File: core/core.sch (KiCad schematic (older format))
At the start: 52 parts, among them J1 Micro_SD_Card, J2 UART_DEBUG, J3 Conn_ARM_JTAG_SWD_10, J4 Conn_01x02, J5 USB_OTG, SW1 SW_Push, SW2 SW_Push, U1 SC18IS600, U2 AP1509-50, U3 AP1509-33

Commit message: update layout
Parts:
- removed TP1, TP10, TP11, TP5, TP7: TestPoint, TestPoint:TestPoint_Keystone_5010-5014_Multipurpose, symbol Connector:TestPoint
- J2: footprint star-common-lib:TSM-103-01-L-SV -> Connector_PinHeader_2.54mm:PinHeader_1x03_P2.54mm_Vertical; DIGIKEY SAM8981-ND -> 609-3470-ND; MANF TSM-103-01-L-SV -> 68001-203HLF
- SW1, SW2: footprint Button_Switch_SMD:SW_SPST_CK_RS282G05A3 -> Button_Switch_SMD:SW_SPST_PTS810; DIGIKEY CKN10384CT-ND -> CKN10502CT-ND; MANF RS-282G05A3-SM RT -> PTS810 SJM 250 SMTR LFS
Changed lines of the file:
@@
 F 0 "SW1" H 5550 2735 50  0000 C CNN
 F 1 "SW_Push" H 5550 2644 50  0000 C CNN
-F 2 "Button_Switch_SMD:SW_SPST_CK_RS282G05A3" H 5550 2650 50  0001 C CNN
+F 2 "Button_Switch_SMD:SW_SPST_PTS810" H 5550 2650 50  0001 C CNN
 F 3 "~" H 5550 2650 50  0001 C CNN
-F 4 "CKN10384CT-ND" H 5550 2450 50  0001 C CNN "DIGIKEY"
-F 5 "RS-282G05A3-SM RT" H 5550 2450 50  0001 C CNN "MANF"
+F 4 "CKN10502CT-ND" H 5550 2450 50  0001 C CNN "DIGIKEY"
+F 5 "PTS810 SJM 250 SMTR LFS" H 5550 2450 50  0001 C CNN "MANF"
 	1    5550 2450
 	1    0    0    -1
@@
 F 0 "J2" H 3758 3181 50  0000 C CNN
 F 1 "UART_DEBUG" H 3758 3090 50  0000 C CNN
-F 2 "star-common-lib:TSM-103-01-L-SV" H 3650 2900 50  0001 C CNN
+F 2 "Connector_PinHeader_2.54mm:PinHeader_1x03_P2.54mm_Vertical" H 3650 2900 50  0001 C CNN
 F 3 "~" H 3650 2900 50  0001 C CNN
 F 4 "" H 3650 2900 50  0001 C CNN "manf#"
-F 5 "TSM-103-01-L-SV" H 3650 2900 50  0001 C CNN "MANF"
-F 6 "SAM8981-ND" H 3650 2900 50  0001 C CNN "DIGIKEY"
+F 5 "68001-203HLF" H 3650 2900 50  0001 C CNN "MANF"
+F 6 "609-3470-ND" H 3650 2900 50  0001 C CNN "DIGIKEY"
 	1    3650 2900
 	1    0    0    -1
@@
 Wire Wire Line
 	4600 1650 4750 1650
-$Comp
-L Connector:TestPoint TP1
-U 1 1 5F25E4E9
-P 10200 3750
-F 0 "TP1" H 10258 3868 50  0000 L CNN
-F 1 "TestPoint" H 10258 3777 50  0000 L CNN
-F 2 "TestPoint:TestPoint_Keystone_5010-5014_Multipurpose" H 10400 3750 50  0001 C CNN
-F 3 "~" H 10400 3750 50  0001 C CNN
-F 4 "36-5014-ND" H 10200 3750 50  0001 C CNN "DIGIKEY"
-F 5 "5014" H 10200 3750 50  0001 C CNN "MANF"
-	1    10200 3750
-	-1   0    0    1
-$EndComp
-$Comp
-L power:+3.3V #PWR040
-U 1 1 5F2D6F88
-P 10200 3750
-F 0 "#PWR040" H 10200 3600 50  0001 C CNN
-F 1 "+3.3V" H 10215 3923 50  0000 C CNN
-F 2 "" H 10200 3750 50  0001 C CNN
-F 3 "" H 10200 3750 50  0001 C CNN
-	1    10200 3750
-	1    0    0    -1
-$EndComp
-$Comp
-L Connector:TestPoint TP7
-U 1 1 5F2D875C
-P 10650 3750
-F 0 "TP7" H 10708 3868 50  0000 L CNN
-F 1 "TestPoint" H 10708 3777 50  0000 L CNN
-F 2 "TestPoint:TestPoint_Keystone_5010-5014_Multipurpose" H 10850 3750 50  0001 C CNN
-F 3 "~" H 10850 3750 50  0001 C CNN
-F 4 "36-5014-ND" H 10650 3750 50  0001 C CNN "DIGIKEY"
-F 5 "5014" H 10650 3750 50  0001 C CNN "MANF"
-	1    10650 3750
-	-1   0    0    1
-$EndComp
-$Comp
-L power:+5V #PWR045
-U 1 1 5F2DA0B7
-P 10650 3750
-F 0 "#PWR045" H 10650 3600 50  0001 C CNN
-F 1 "+5V" H 10665 3923 50  0000 C CNN
-F 2 "" H 10650 3750 50  0001 C CNN
-F 3 "" H 10650 3750 50  0001 C CNN
-	1    10650 3750
-	1    0    0    -1
-$EndComp
 Wire Notes Line
 	6900 2750 6900 3500
@@
 F 0 "SW2" H 6450 1735 50  0000 C CNN
 F 1 "SW_Push" H 6450 1644 50  0000 C CNN
-F 2 "Button_Switch_SMD:SW_SPST_CK_RS282G05A3" H 6450 1650 50  0001 C CNN
+F 2 "Button_Switch_SMD:SW_SPST_PTS810" H 6450 1650 50  0001 C CNN
 F 3 "~" H 6450 1650 50  0001 C CNN
-F 4 "CKN10384CT-ND" H 6450 1450 50  0001 C CNN "DIGIKEY"
-F 5 "RS-282G05A3-SM RT" H 6450 1450 50  0001 C CNN "MANF"
+F 4 "CKN10502CT-ND" H 6450 1450 50  0001 C CNN "DIGIKEY"
+F 5 "PTS810 SJM 250 SMTR LFS" H 6450 1450 50  0001 C CNN "MANF"
 	1    6450 1450
 	1    0    0    -1
@@
 Text Label 10650 5450 0    50   ~ 0
 I2C3_SCL
-$Comp
-L Connector:TestPoint TP10
-U 1 1 5F7F994C
-P 10650 4800
-F 0 "TP10" H 10708 4918 50  0000 L CNN
-F 1 "TestPoint" H 10708 4827 50  0000 L CNN
-F 2 "TestPoint:TestPoint_Keystone_5010-5014_Multipurpose" H 10850 4800 50  0001 C CNN
-F 3 "~" H 10850 4800 50  0001 C CNN
-F 4 "36-5014-ND" H 10650 4800 50  0001 C CNN "DIGIKEY"
-F 5 "5014" H 10650 4800 50  0001 C CNN "MANF"
-	1    10650 4800
-	-1   0    0    1
-$EndComp
-$Comp
-L Connector:TestPoint TP5
-U 1 1 5F7F9952
-P 10200 5150
-F 0 "TP5" H 10258 5268 50  0000 L CNN
-F 1 "TestPoint" H 10258 5177 50  0000 L CNN
-F 2 "TestPoint:TestPoint_Keystone_5010-5014_Multipurpose" H 10400 5150 50  0001 C CNN
-F 3 "~" H 10400 5150 50  0001 C CNN
-F 4 "36-5014-ND" H 10200 5150 50  0001 C CNN "DIGIKEY"
-F 5 "5014" H 10200 5150 50  0001 C CNN "MANF"
-	1    10200 5150
-	-1   0    0    1
-$EndComp
-$Comp
-L Connector:TestPoint TP11
-U 1 1 5F7F9958
-P 10650 5150
-F 0 "TP11" H 10708 5268 50  0000 L CNN
-F 1 "TestPoint" H 10708 5177 50  0000 L CNN
-F 2 "TestPoint:TestPoint_Keystone_5010-5014_Multipurpose" H 10850 5150 50  0001 C CNN
-F 3 "~" H 10850 5150 50  0001 C CNN
-F 4 "36-5014-ND" H 10650 5150 50  0001 C CNN "DIGIKEY"
-F 5 "5014" H 10650 5150 50  0001 C CNN "MANF"
-	1    10650 5150
-	-1   0    0    1
-$EndComp
-Text Label 10650 4750 0    50   ~ 0
-USB_VBUS
-Text Label 10200 5100 0    50   ~ 0
-USB_DP
-Text Label 10650 5100 0    50   ~ 0
-USB_DM
 Wire Wire Line
 	10200 4050 10200 4100
@@
 Wire Wire Line
 	10200 4750 10200 4800
-Wire Wire Line
-	10650 4750 10650 4800
-Wire Wire Line
-	10200 5100 10200 5150
-Wire Wire Line
-	10650 5100 10650 5150
 NoConn ~ 8000 5150
 Wire Wire Line

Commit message: Second Layout pass on core
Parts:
- TP2, TP3, TP4, TP8, TP9: footprint TestPoint:TestPoint_Keystone_5010-5014_Multipurpose -> TestPoint:TestPoint_Keystone_5019_Minature; DIGIKEY 36-5014-ND -> 36-5019CT-ND; MANF 5014 -> 5019
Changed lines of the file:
@@
 F 0 "TP2" H 10258 4218 50  0000 L CNN
 F 1 "TestPoint" H 10258 4127 50  0000 L CNN
-F 2 "TestPoint:TestPoint_Keystone_5010-5014_Multipurpose" H 10400 4100 50  0001 C CNN
+F 2 "TestPoint:TestPoint_Keystone_5019_Minature" H 10400 4100 50  0001 C CNN
 F 3 "~" H 10400 4100 50  0001 C CNN
-F 4 "36-5014-ND" H 10200 4100 50  0001 C CNN "DIGIKEY"
-F 5 "5014" H 10200 4100 50  0001 C CNN "MANF"
+F 4 "36-5019CT-ND" H 10200 4100 50  0001 C CNN "DIGIKEY"
+F 5 "5019" H 10200 4100 50  0001 C CNN "MANF"
 	1    10200 4100
 	-1   0    0    1
@@
 F 0 "TP8" H 10708 4218 50  0000 L CNN
 F 1 "TestPoint" H 10708 4127 50  0000 L CNN
-F 2 "TestPoint:TestPoint_Keystone_5010-5014_Multipurpose" H 10850 4100 50  0001 C CNN
+F 2 "TestPoint:TestPoint_Keystone_5019_Minature" H 10850 4100 50  0001 C CNN
 F 3 "~" H 10850 4100 50  0001 C CNN
-F 4 "36-5014-ND" H 10650 4100 50  0001 C CNN "DIGIKEY"
-F 5 "5014" H 10650 4100 50  0001 C CNN "MANF"
+F 4 "36-5019CT-ND" H 10650 4100 50  0001 C CNN "DIGIKEY"
+F 5 "5019" H 10650 4100 50  0001 C CNN "MANF"
 	1    10650 4100
 	-1   0    0    1
@@
 F 0 "TP3" H 10258 4568 50  0000 L CNN
 F 1 "TestPoint" H 10258 4477 50  0000 L CNN
-F 2 "TestPoint:TestPoint_Keystone_5010-5014_Multipurpose" H 10400 4450 50  0001 C CNN
+F 2 "TestPoint:TestPoint_Keystone_5019_Minature" H 10400 4450 50  0001 C CNN
 F 3 "~" H 10400 4450 50  0001 C CNN
-F 4 "36-5014-ND" H 10200 4450 50  0001 C CNN "DIGIKEY"
-F 5 "5014" H 10200 4450 50  0001 C CNN "MANF"
+F 4 "36-5019CT-ND" H 10200 4450 50  0001 C CNN "DIGIKEY"
+F 5 "5019" H 10200 4450 50  0001 C CNN "MANF"
 	1    10200 4450
 	-1   0    0    1
@@
 F 0 "TP9" H 10708 4568 50  0000 L CNN
 F 1 "TestPoint" H 10708 4477 50  0000 L CNN
-F 2 "TestPoint:TestPoint_Keystone_5010-5014_Multipurpose" H 10850 4450 50  0001 C CNN
+F 2 "TestPoint:TestPoint_Keystone_5019_Minature" H 10850 4450 50  0001 C CNN
 F 3 "~" H 10850 4450 50  0001 C CNN
-F 4 "36-5014-ND" H 10650 4450 50  0001 C CNN "DIGIKEY"
-F 5 "5014" H 10650 4450 50  0001 C CNN "MANF"
+F 4 "36-5019CT-ND" H 10650 4450 50  0001 C CNN "DIGIKEY"
+F 5 "5019" H 10650 4450 50  0001 C CNN "MANF"
 	1    10650 4450
 	-1   0    0    1
@@
 F 0 "TP4" H 10258 4918 50  0000 L CNN
 F 1 "TestPoint" H 10258 4827 50  0000 L CNN
-F 2 "TestPoint:TestPoint_Keystone_5010-5014_Multipurpose" H 10400 4800 50  0001 C CNN
+F 2 "TestPoint:TestPoint_Keystone_5019_Minature" H 10400 4800 50  0001 C CNN
 F 3 "~" H 10400 4800 50  0001 C CNN
-F 4 "36-5014-ND" H 10200 4800 50  0001 C CNN "DIGIKEY"
-F 5 "5014" H 10200 4800 50  0001 C CNN "MANF"
+F 4 "36-5019CT-ND" H 10200 4800 50  0001 C CNN "DIGIKEY"
+F 5 "5019" H 10200 4800 50  0001 C CNN "MANF"
 	1    10200 4800
 	-1   0    0    1

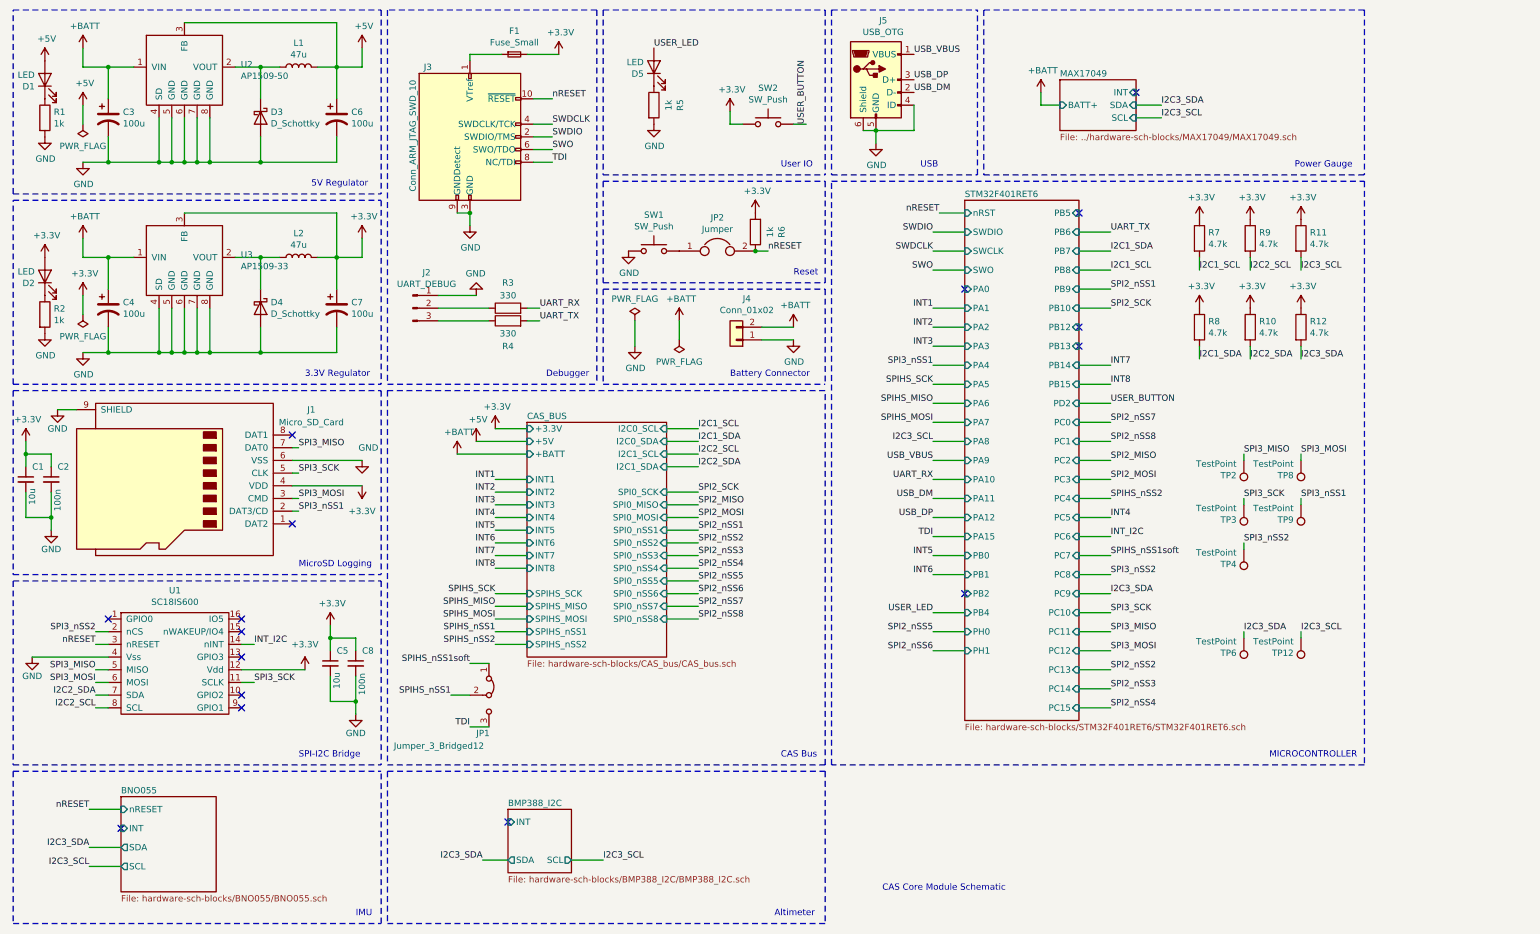
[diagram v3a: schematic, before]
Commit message: update schematic
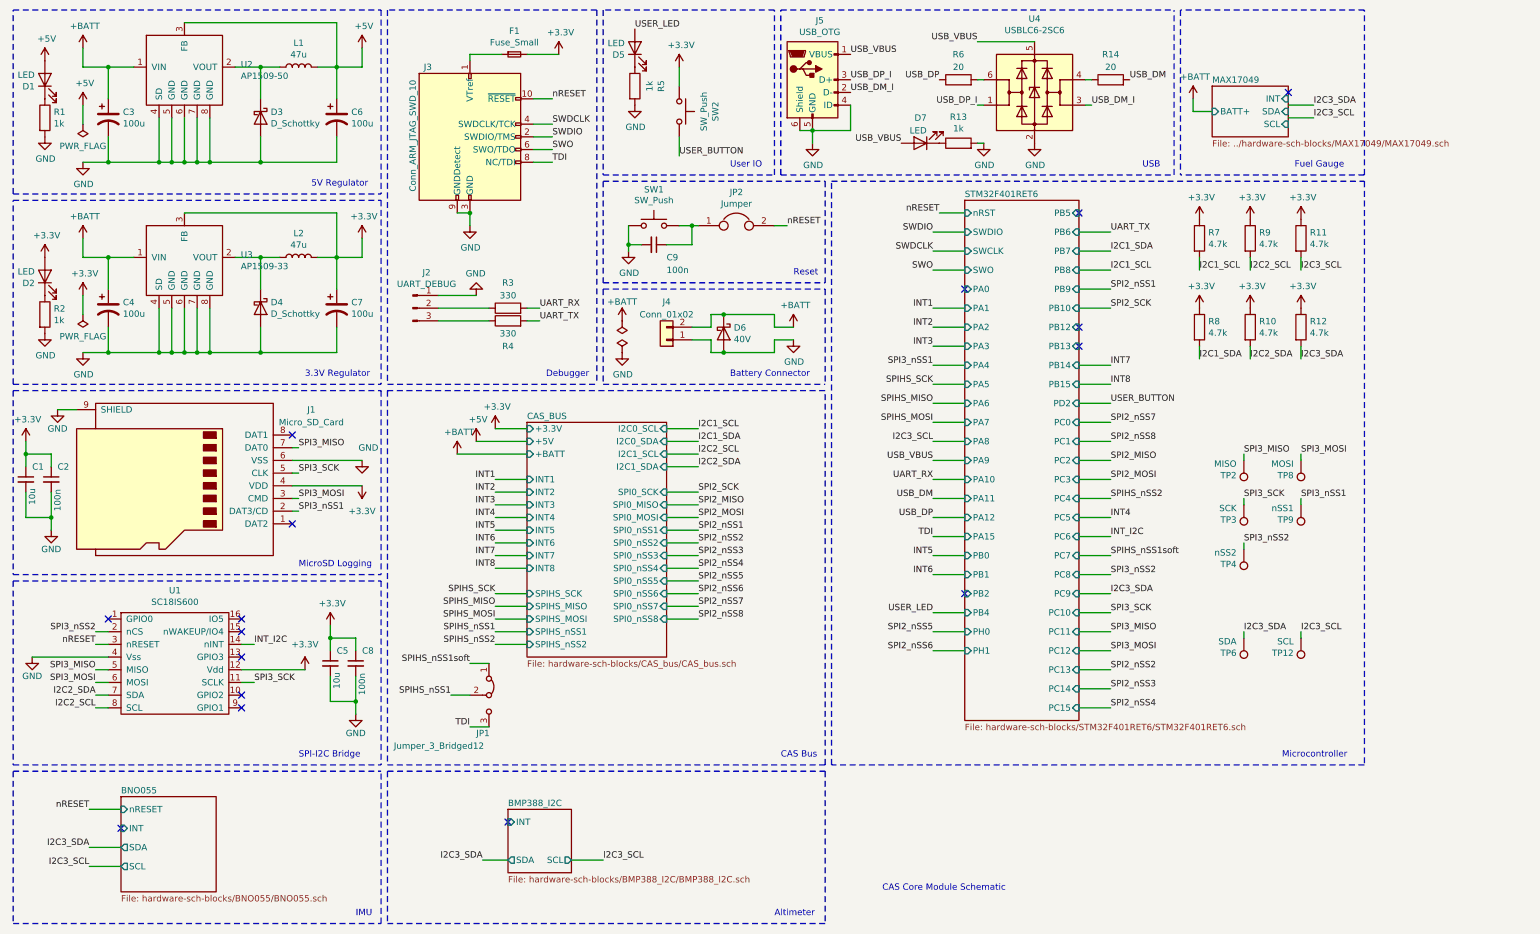
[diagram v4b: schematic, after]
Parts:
- added C9: 100n, Capacitor_SMD:C_0603_1608Metric, symbol Device:C_Small
- added D6: 40V, Diode_SMD:D_0603_1608Metric, symbol Device:D_Schottky
- added D7: LED, LED_SMD:LED_0603_1608Metric, symbol Device:LED
- added R13: 1k, Resistor_SMD:R_0603_1608Metric, symbol Device:R
- added R14: 20, Resistor_SMD:R_0603_1608Metric, symbol Device:R
- added U4: USBLC6-2SC6, Package_TO_SOT_SMD:SOT-23-6, symbol Power_Protection:USBLC6-2SC6
- R6: value 1k -> 20; DIGIKEY 311-1.0KGRCT-ND -> 311-20.0HRTR-ND; MANF RC0603JR-071KL -> RC0603FR-0720RL
- TP12: value TestPoint -> SCL
- TP2: value TestPoint -> MISO
- TP3: value TestPoint -> SCK
- TP4: value TestPoint -> nSS2
- TP6: value TestPoint -> SDA
- TP8: value TestPoint -> MOSI
- TP9: value TestPoint -> nSS1
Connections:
- net +3V3: no longer R6.2
- net +BATT: now also D6.1 (K)
- net GND: now also C9.2, D6.2 (A), R13.2, U4.2 (GND)
- net USB_DM: now also R14.2; no longer J5.2 (D-)
- net USB_DP: now also R6.1; no longer J5.3 (D+)
- net USB_VBUS: now also D7.2 (A), U4.5 (VBUS)
- net nRESET: no longer R6.1
- net at JP2.1, SW1.2: now also C9.1
- new net: R6.2, U4.6 (I/O1)
- new net: R14.1, U4.4 (I/O2)
- new net: D7.1 (K), R13.1
- new net USB_DM_I: J5.2 (D-), U4.3 (I/O2)
- new net USB_DP_I: J5.3 (D+), U4.1 (I/O1)
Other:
- note added: "Fuel Gauge"
- note added: "Microcontroller"
- note removed: "MICROCONTROLLER"
- note removed: "Power Gauge"
- moved on the sheet: D5, J4, J5, JP2, R5, SW1, SW2

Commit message: made layout revisions
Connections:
- net USB_DM: now also R6.1; no longer R14.2
- net USB_DM_I: now also U4.1 (I/O1); no longer U4.3 (I/O2)
- net USB_DP: now also R14.2; no longer R6.1
- net USB_DP_I: now also U4.3 (I/O2); no longer U4.1 (I/O1)
- no-connect marks 16 -> 17
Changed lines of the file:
@@
 Text Label 5900 3950 0    50   ~ 0
 I2C1_SDA
-Text Label 10750 1400 0    50   ~ 0
+Text Label 10750 1450 0    50   ~ 0
 I2C3_SCL
-Text Label 10750 1300 0    50   ~ 0
+Text Label 10750 1350 0    50   ~ 0
 I2C3_SDA
 Text Label 9150 5150 0    50   ~ 0
@@
 F3 "SDA" O L 4400 7250 50
 F4 "SCL" O R 4900 7250 50
+F5 "CSB" I R 4900 6950 50
 $EndSheet
 Wire Wire Line
@@
 Wire Wire Line
 	4900 7250 5150 7250
-Wire Wire Line
-	10750 1400 10550 1400
 Text Label 5900 4050 0    50   ~ 0
 I2C2_SCL
-Wire Wire Line
-	10550 1300 10750 1300
 Text Label 5900 4150 0    50   ~ 0
 I2C2_SDA
@@
 Text Label 7100 1100 0    50   ~ 0
 USB_DP_I
-Text Label 9300 1100 0    50   ~ 0
+Text Label 7800 1100 2    50   ~ 0
 USB_DM
 Text Label 7750 4550 2    50   ~ 0
@@
 NoConn ~ 1350 7000
 NoConn ~ 4400 6950
-NoConn ~ 10550 1200
 Text Label 4200 7250 2    50   ~ 0
 I2C3_SDA
@@
 Wire Wire Line
 	8950 1300 9000 1300
-Text Label 7800 1100 2    50   ~ 0
+Text Label 9300 1100 0    50   ~ 0
 USB_DP
 Wire Wire Line
@@
 Wire Wire Line
 	8100 800  8550 800
+Text Label 8100 1300 2    50   ~ 0
+USB_DM_I
 Text Label 9000 1300 0    50   ~ 0
-USB_DM_I
-Text Label 8100 1300 2    50   ~ 0
 USB_DP_I
 $Comp
@@
 	0    -1   -1   0
 $EndComp
+NoConn ~ 4900 6950
+NoConn ~ 10550 1250
+Wire Wire Line
+	10750 1350 10550 1350
+Wire Wire Line
+	10550 1450 10750 1450
 $EndSCHEMATC

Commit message: update silk
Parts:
- JP2: value Jumper -> RST_JUMP
- SW1: value SW_Push -> RESET
- SW2: value SW_Push -> USER
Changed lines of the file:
@@
 P 5550 2250
 F 0 "SW1" H 5550 2535 50  0000 C CNN
-F 1 "SW_Push" H 5550 2450 50  0000 C CNN
+F 1 "RESET" H 5550 2450 50  0000 C CNN
 F 2 "Button_Switch_SMD:SW_SPST_PTS810" H 5550 2450 50  0001 C CNN
 F 3 "~" H 5550 2450 50  0001 C CNN
@@
 P 6200 2250
 F 0 "JP2" H 6200 2514 50  0000 C CNN
-F 1 "Jumper" H 6200 2423 50  0000 C CNN
+F 1 "RST_JUMP" H 6200 2423 50  0000 C CNN
 F 2 "Connector_PinHeader_2.54mm:PinHeader_1x02_P2.54mm_Vertical" H 6200 2250 50  0001 C CNN
 F 3 "~" H 6200 2250 50  0001 C CNN
@@
 P 5750 1350
 F 0 "SW2" H 5750 1635 50  0000 C CNN
-F 1 "SW_Push" H 5750 1544 50  0000 C CNN
+F 1 "USER" H 5750 1544 50  0000 C CNN
 F 2 "Button_Switch_SMD:SW_SPST_PTS810" H 5750 1550 50  0001 C CNN
 F 3 "~" H 5750 1550 50  0001 C CNN

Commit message: fix silk
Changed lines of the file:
@@
 U 1 1 5EC9ED5D
 P 1850 950
-F 0 "U2" H 2294 921 50  0000 L CNN
-F 1 "AP1509-50" H 2294 830 50  0000 L CNN
+F 0 "U2" H 2200 1150 50  0000 L CNN
+F 1 "AP1509-50" H 2200 1050 50  0000 L CNN
 F 2 "Package_SO:SO-8_3.9x4.9mm_P1.27mm" H 1900 1300 50  0001 C CNN
 F 3 "https://www.diodes.com/assets/Datasheets/AP1509.pdf" H 1900 1300 50  0001 C CNN
@@
 U 1 1 5ECE6C92
 P 1850 2450
-F 0 "U3" H 2294 2421 50  0000 L CNN
-F 1 "AP1509-33" H 2294 2330 50  0000 L CNN
+F 0 "U3" H 2200 2650 50  0000 L CNN
+F 1 "AP1509-33" H 2200 2550 50  0000 L CNN
 F 2 "Package_SO:SO-8_3.9x4.9mm_P1.27mm" H 1900 2800 50  0001 C CNN
 F 3 "https://www.diodes.com/assets/Datasheets/AP1509.pdf" H 1900 2800 50  0001 C CNN
